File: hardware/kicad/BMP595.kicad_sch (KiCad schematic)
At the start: 4 parts, among them U301 BMP585

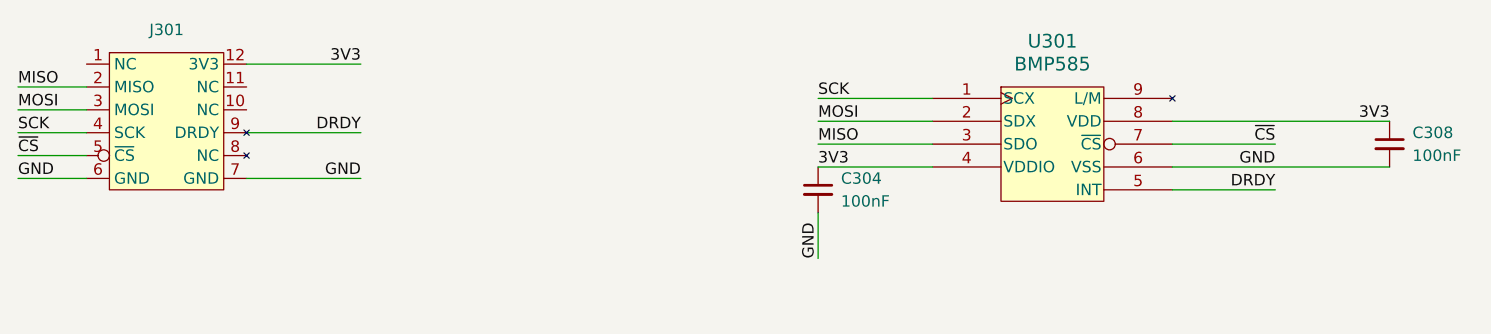
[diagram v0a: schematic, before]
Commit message: Moved sensors from stamp to direct placement
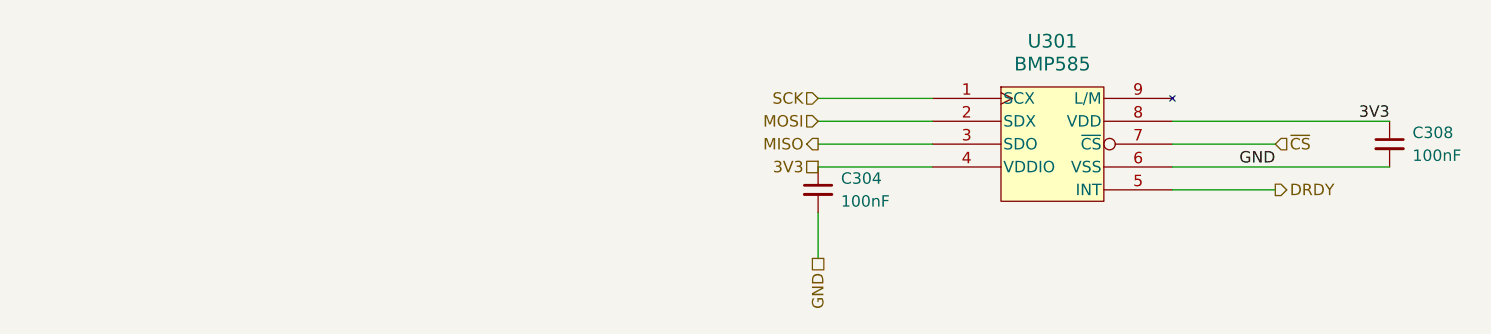
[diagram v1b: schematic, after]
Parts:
- removed J301: (no value), footprints:Stamp, symbol rollercoasterometer2026:STAMP
